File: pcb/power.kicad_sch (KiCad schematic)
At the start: 60 parts, among them J7 1S LiPo, Q1 Q_Dual_NMOS_S1G1S2G2D2D2D1D1, Q2 Q_Dual_NMOS_S1G1S2G2D2D2D1D1, Q3 Q_Dual_NMOS_S1G1S2G2D2D2D1D1, U13 BQ25798, U14 TPS63060, U15 TPS61089

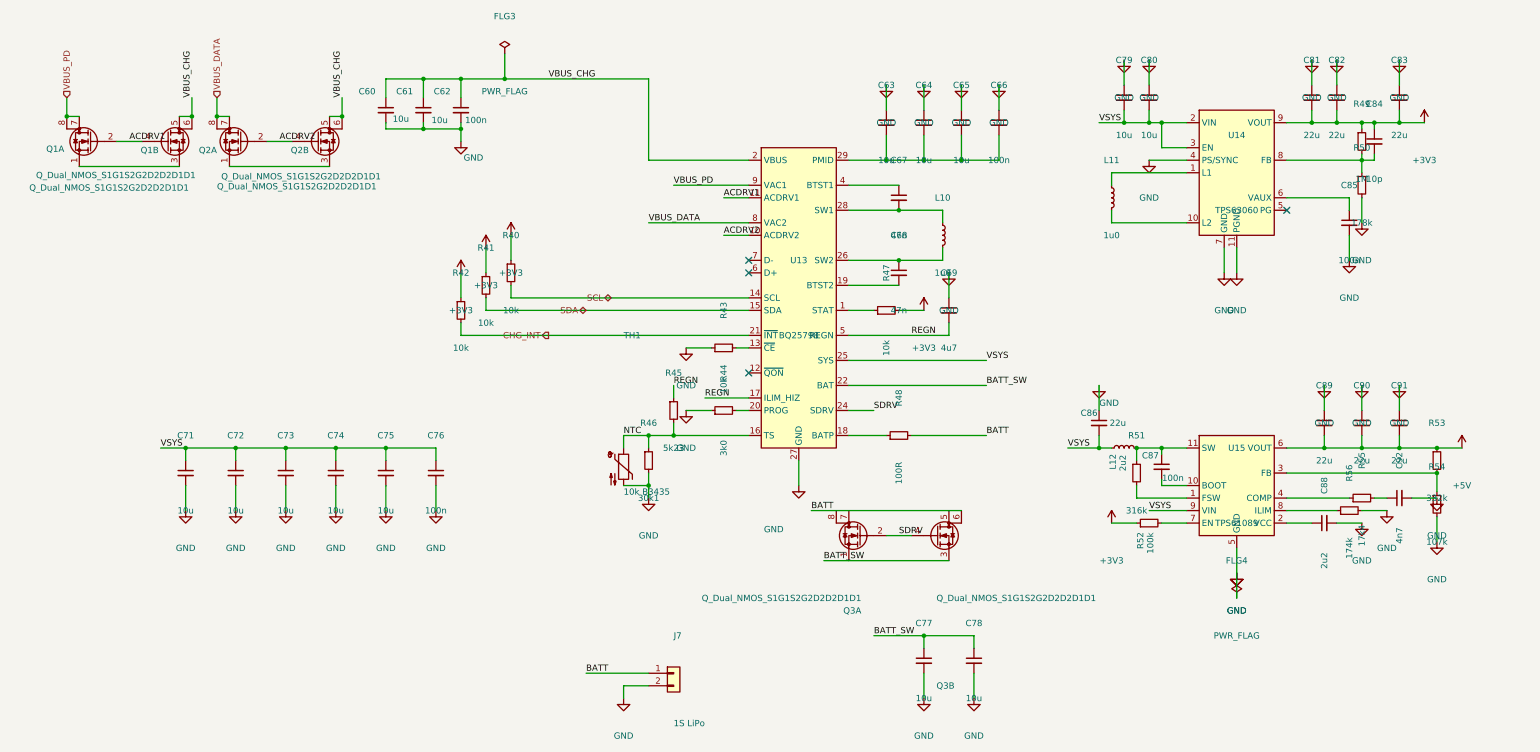
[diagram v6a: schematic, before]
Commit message: calculate the capacitor banks, and give every one of them a package
The question a value and a rating leave open is how much capacitance is actually there once the
voltage is across it, and the answer differs by package for the same value and rating. So the
requirement is derived bank by bank rather than taken from the vendors' part counts.

The charger's input is the binding case. Holding its input ripple to 100 mV with 5.4 A through the
inductor needs 8.6uF in circuit out of the 20uF fitted, so 43% has to survive 9V. The 5V rail needs
36% of what it carries and the system rail 27%. That last one is worth stating properly: ripple
alone would want only 2.5uF there, so the bank exists to answer load steps, and the realistic fast
step is the radio transmitting and the processor waking rather than the ports, which cannot step
quickly because the boost soft-starts over 4ms. At half an amp over five microseconds that is 25uF
against about 70uF effective.

43% is comfortable in 1206 and marginal in 0603 for a 10uF part at 9V, so the five capacitors on
the 9V nodes take 1206 and everything at 4.5V or under takes 0805. Decoupling goes to 0402, where
being near the pin matters more than the package, and the frequency- and loop-setting parts to
0603, where there is nothing to derate.

The answer to the open item is that the counts do not change: every bank is adequate as drawn
provided each part keeps roughly half of itself, which is what the package choice delivers. What is
left is a purchasing check rather than a design one.

Two asymmetries recorded. The 3.3V converter's vendor states that its recommended values anticipate
tolerance and bias derating and quotes 20% and 50%, so its table is nominal with the margin already
in it; the charger's and the boost's say nothing, so there the derating is ours to carry. And the
processor specifies an effective tolerance rather than a nominal one -- its core regulator's output
capacitor must be 4.7uF +/-20% in circuit.

The checker's 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
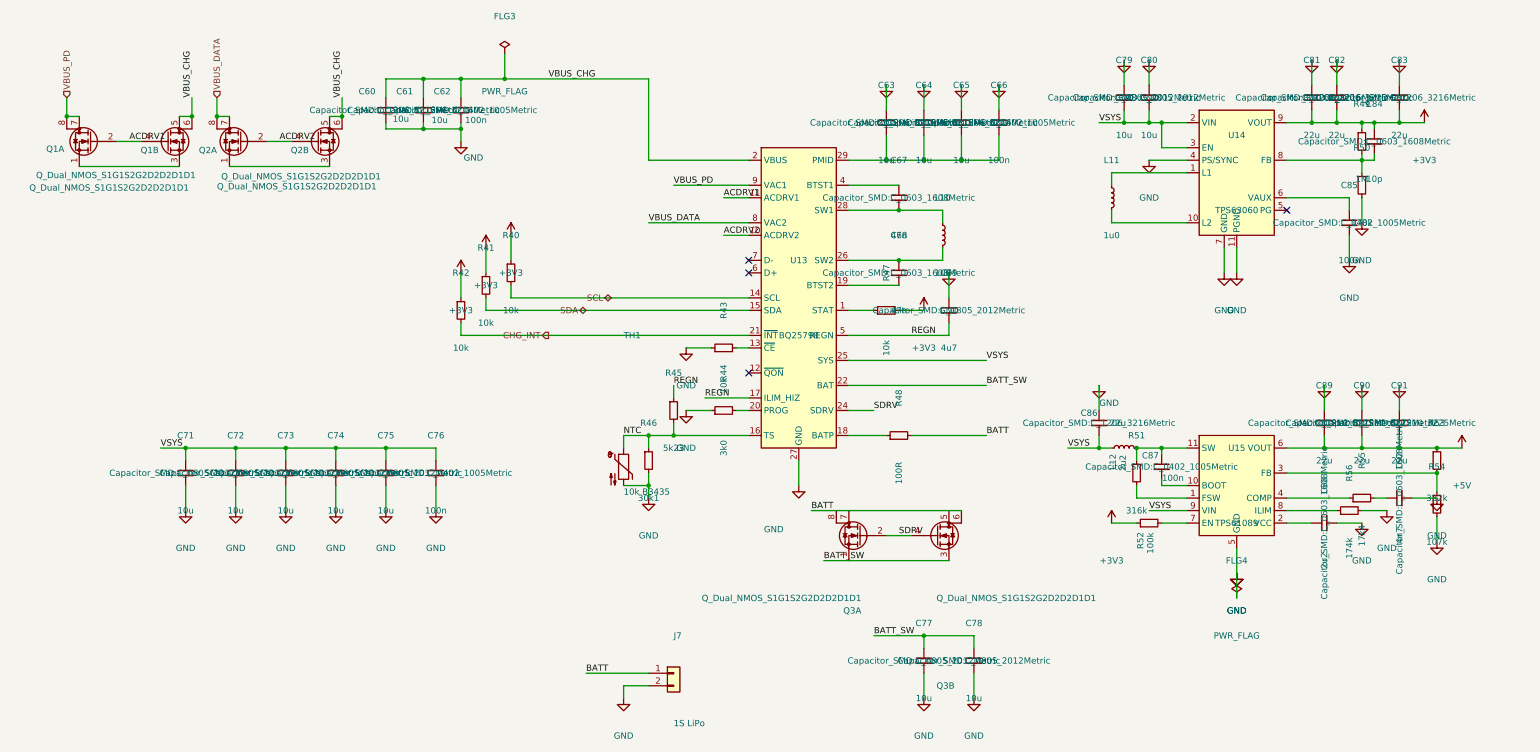
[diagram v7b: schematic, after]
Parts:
- C60, C61, C63, C64, C65, C81, C82, C83, C86: footprint (none) -> Capacitor_SMD:C_1206_3216Metric
- C62, C66, C76, C85, C87: footprint (none) -> Capacitor_SMD:C_0402_1005Metric
- C67, C68, C84, C88, C92: footprint (none) -> Capacitor_SMD:C_0603_1608Metric
- C69, C71, C72, C73, C74, C75, C77, C78, C79, C80: footprint (none) -> Capacitor_SMD:C_0805_2012Metric
- C89, C90, C91: footprint (none) -> Capacitor_SMD:C_1210_3225Metric
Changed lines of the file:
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@@
 			)
 		)
-		(property "Footprint" ""
+		(property "Footprint" "Capacitor_SMD:C_0805_2012Metric"
 			(at 248.92 86.36 0)
 			(show_name no)
@@
 			)
 		)
-		(property "Footprint" ""
+		(property "Footprint" "Capacitor_SMD:C_1206_3216Metric"
 			(at 287.02 86.36 0)
 			(show_name no)
@@
 			)
 		)
-		(property "Footprint" ""
+		(property "Footprint" "Capacitor_SMD:C_0402_1005Metric"
 			(at 289.56 111.76 0)
 			(show_name no)
@@
 			)
 		)
-		(property "Footprint" ""
+		(property "Footprint" "Capacitor_SMD:C_0603_1608Metric"
 			(at 284.48 172.72 0)
 			(show_name no)
@@
 			)
 		)
-		(property "Footprint" ""
+		(property "Footprint" "Capacitor_SMD:C_1206_3216Metric"
 			(at 238.76 152.4 0)
 			(show_name no)
@@
 			)
 		)
-		(property "Footprint" ""
+		(property "Footprint" "Capacitor_SMD:C_1210_3225Metric"
 			(at 284.48 152.4 0)
 			(show_name no)
@@
 			)
 		)
-		(property "Footprint" ""
+		(property "Footprint" "Capacitor_SMD:C_0805_2012Metric"
 			(at 203.2 200.66 0)
 			(show_name no)
@@
 			)
 		)
-		(property "Footprint" ""
+		(property "Footprint" "Capacitor_SMD:C_0603_1608Metric"
 			(at 294.64 95.25 0)
 			(show_name no)
@@
 			)
 		)
-		(property "Footprint" ""
+		(property "Footprint" "Capacitor_SMD:C_0805_2012Metric"
 			(at 83.82 162.56 0)
 			(show_name no)
@@
 			)
 		)
-		(property "Footprint" ""
+		(property "Footprint" "Capacitor_SMD:C_0402_1005Metric"
 			(at 104.14 162.56 0)
 			(show_name no)
@@
 			)
 		)
-		(property "Footprint" ""
+		(property "Footprint" "Capacitor_SMD:C_1210_3225Metric"
 			(at 299.72 152.4 0)
 			(show_name no)
@@
 			)
 		)
-		(property "Footprint" ""
+		(property "Footprint" "Capacitor_SMD:C_0805_2012Metric"
 			(at 73.66 162.56 0)
 			(show_name no)
@@
 			)
 		)
-		(property "Footprint" ""
+		(property "Footprint" "Capacitor_SMD:C_0402_1005Metric"
 			(at 251.46 161.29 0)
 			(show_name no)
@@
 			)
 		)
-		(property "Footprint" ""
+		(property "Footprint" "Capacitor_SMD:C_1206_3216Metric"
 			(at 195.58 91.44 0)
 			(show_name no)
@@
 			)
 		)
-		(property "Footprint" ""
+		(property "Footprint" "Capacitor_SMD:C_0805_2012Metric"
 			(at 243.84 86.36 0)
 			(show_name no)
@@
 			)
 		)
-		(property "Footprint" ""
+		(property "Footprint" "Capacitor_SMD:C_1210_3225Metric"
 			(at 292.1 152.4 0)
 			(show_name no)
@@
 			)
 		)
-		(property "Footprint" ""
+		(property "Footprint" "Capacitor_SMD:C_0402_1005Metric"
 			(at 218.44 91.44 0)
 			(show_name no)
@@
 			)
 		)
-		(property "Footprint" ""
+		(property "Footprint" "Capacitor_SMD:C_1206_3216Metric"
 			(at 93.98 88.9 0)
 			(show_name no)
@@
 			)
 		)
-		(property "Footprint" ""
+		(property "Footprint" "Capacitor_SMD:C_0805_2012Metric"
 			(at 93.98 162.56 0)
 			(show_name no)
@@
 			)
 		)
-		(property "Footprint" ""
+		(property "Footprint" "Capacitor_SMD:C_1206_3216Metric"
 			(at 203.2 91.44 0)
 			(show_name no)
@@
 			)
 		)
-		(property "Footprint" ""
+		(property "Footprint" "Capacitor_SMD:C_0402_1005Metric"
 			(at 109.22 88.9 0)
 			(show_name no)
@@
 			)
 		)
-		(property "Footprint" ""
+		(property "Footprint" "Capacitor_SMD:C_0805_2012Metric"
 			(at 53.34 162.56 0)
 			(show_name no)
@@
 			)
 		)
-		(property "Footprint" ""
+		(property "Footprint" "Capacitor_SMD:C_0805_2012Metric"
 			(at 213.36 200.66 0)
 			(show_name no)
@@
 			)
 		)
-		(property "Footprint" ""
+		(property "Footprint" "Capacitor_SMD:C_1206_3216Metric"
 			(at 299.72 86.36 0)
 			(show_name no)
@@
 			)
 		)
-		(property "Footprint" ""
+		(property "Footprint" "Capacitor_SMD:C_0603_1608Metric"
 			(at 299.72 167.64 0)
 			(show_name no)
@@
 			)
 		)
-		(property "Footprint" ""
+		(property "Footprint" "Capacitor_SMD:C_0805_2012Metric"
 			(at 208.28 129.54 0)
 			(show_name no)
@@
 			)
 		)
-		(property "Footprint" ""
+		(property "Footprint" "Capacitor_SMD:C_1206_3216Metric"
 			(at 281.94 86.36 0)
 			(show_name no)
@@
 			)
 		)
-		(property "Footprint" ""
+		(property "Footprint" "Capacitor_SMD:C_0805_2012Metric"
 			(at 63.5 162.56 0)
 			(show_name no)
@@
 			)
 		)
-		(property "Footprint" ""
+		(property "Footprint" "Capacitor_SMD:C_1206_3216Metric"
 			(at 101.6 88.9 0)
 			(show_name no)
@@
 			)
 		)
-		(property "Footprint" ""
+		(property "Footprint" "Capacitor_SMD:C_1206_3216Metric"
 			(at 210.82 91.44 0)
 			(show_name no)
@@
 			)
 		)
-		(property "Footprint" ""
+		(property "Footprint" "Capacitor_SMD:C_0603_1608Metric"
 			(at 198.12 106.68 0)
 			(show_name no)
@@
 			)
 		)
-		(property "Footprint" ""
+		(property "Footprint" "Capacitor_SMD:C_0603_1608Metric"
 			(at 198.12 121.92 0)
 			(show_name no)

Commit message: assign the footprints, and take the radio module's from its vendor
132 of the 135 parts now carry a footprint. Most follow from the package, the capacitors' follow
from the bias calculation, and the resistors are 0603 rather than 0402 because the board has room,
the first one runs bare on a bench, and a part you can get a probe or an iron onto is worth more
there than the millimetre it saves.

The radio module nearly went in hand-drawn. It has no footprint in any stock library, so the
obvious move was to draw one from the dimension drawing in its datasheet; the pitch, pad size and
pad length read off cleanly, but where each pad sits along its edge did not, and what I had was
inference from where things appeared in a rendered figure rather than a stated number. Raspberry Pi
publish a KiCad symbol and footprint, so that is what is fitted, in a project footprint library
beside the project symbol library. The figure agreed on everything it stated plainly, which says
nothing about the parts it did not.

Taking the official symbol also checked this project's hand-drawn one against theirs. All 21 pins
agree. Four carry different names -- their DI and DO, their nIRQ and WL_ON -- and nothing else
differs, so the pin numbering derived from the module's table is confirmed against its author
rather than merely self-consistent.

Four packages are fitted provisionally and are recorded as such, because what is unsettled about
them is invisible: the processor, the hub, the 3.3V converter and the power sink are in packages
whose library entries differ only in the size of the pad under the part. Body, pitch and pin count
are right; the pad is the nearest variant and wants checking against each vendor's land pattern,
since too small costs thermal performance and too large can wick the part off its pins.

Three parts are deliberately left without one. For the remaining inductors the footprint is the
part -- pad geometry differs between vendors at the same nominal size -- so choosing an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
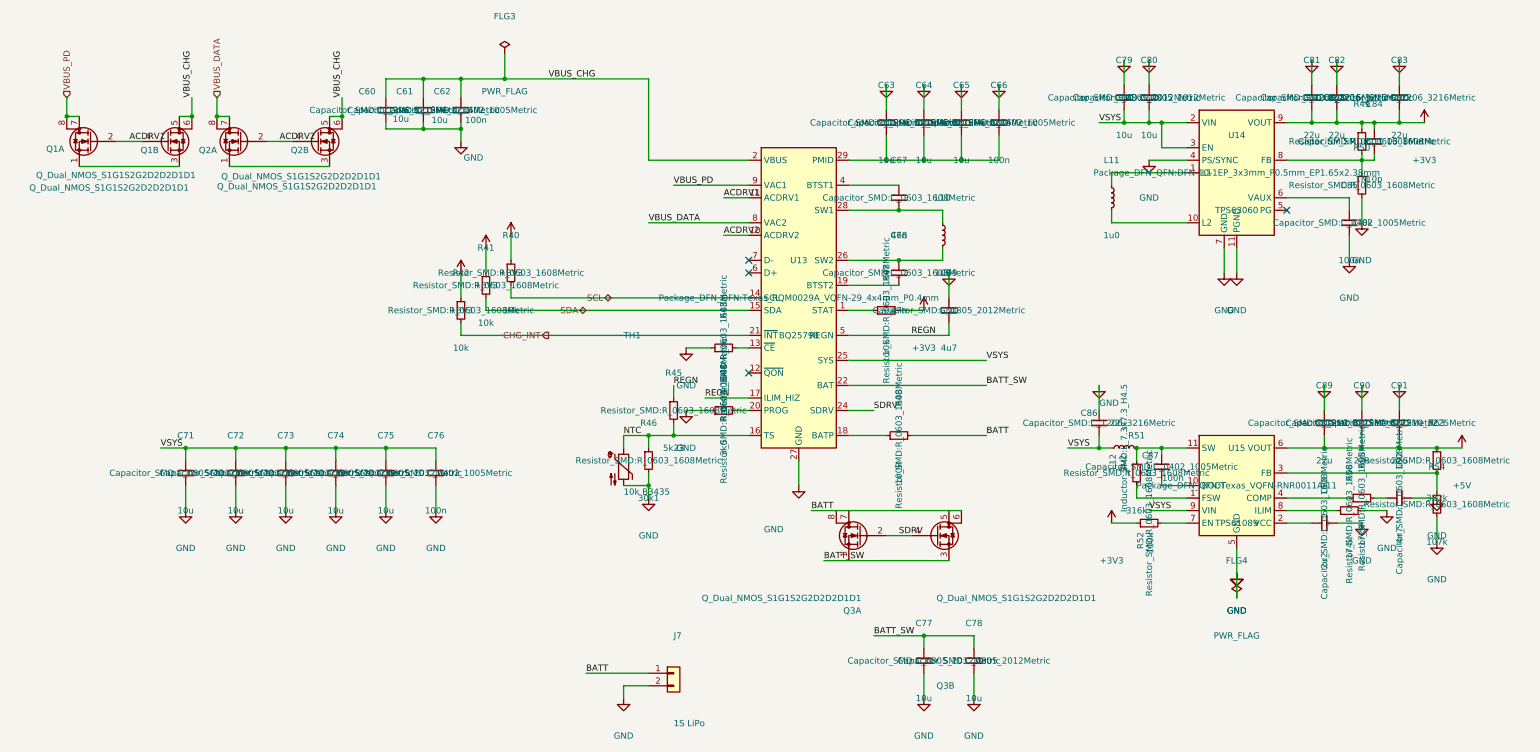
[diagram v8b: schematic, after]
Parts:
- J7: footprint (none) -> Connector_JST:JST_PH_B2B-PH-K_1x02_P2.00mm_Vertical
- L12: footprint (none) -> Inductor_SMD:L_7.3x7.3_H4.5
- Q1, Q2, Q3: footprint (none) -> Package_SO:SOIC-8_3.9x4.9mm_P1.27mm
- R40, R41, R42, R43, R44, R45, R46, R47, R48, R49, R50, R51, R52, R53, R54, R55, R56, TH1: footprint (none) -> Resistor_SMD:R_0603_1608Metric
- U13: footprint (none) -> Package_DFN_QFN:Texas_RQM0029A_VQFN-29_4x4mm_P0.4mm
- U14: footprint (none) -> Package_DFN_QFN:DFN-10-1EP_3x3mm_P0.5mm_EP1.65x2.38mm
- U15: footprint (none) -> Package_DFN_QFN:Texas_VQFN-RNR0011A-11
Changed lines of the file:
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@@
 			)
 		)
-		(property "Footprint" ""
+		(property "Footprint" "Resistor_SMD:R_0603_1608Metric"
 			(at 307.34 160.02 0)
 			(show_name no)
@@
 			)
 		)
-		(property "Footprint" ""
+		(property "Footprint" "Resistor_SMD:R_0603_1608Metric"
 			(at 248.92 172.72 0)
 			(show_name no)
@@
 			)
 		)
-		(property "Footprint" ""
+		(property "Footprint" "Resistor_SMD:R_0603_1608Metric"
 			(at 119.38 121.92 0)
 			(show_name no)
@@
 			)
 		)
-		(property "Footprint" ""
+		(property "Footprint" "Package_SO:SOIC-8_3.9x4.9mm_P1.27mm"
 			(at 34.29 95.25 0)
 			(hide yes)
@@
 			)
 		)
-		(property "Footprint" ""
+		(property "Footprint" "Resistor_SMD:R_0603_1608Metric"
 			(at 152.4 149.86 0)
 			(show_name no)
@@
 			)
 		)
-		(property "Footprint" ""
+		(property "Footprint" "Resistor_SMD:R_0603_1608Metric"
 			(at 292.1 95.25 0)
 			(show_name no)
@@
 			)
 		)
-		(property "Footprint" ""
+		(property "Footprint" "Resistor_SMD:R_0603_1608Metric"
 			(at 292.1 167.64 0)
 			(show_name no)
@@
 			)
 		)
-		(property "Footprint" ""
+		(property "Footprint" "Package_SO:SOIC-8_3.9x4.9mm_P1.27mm"
 			(at 64.77 95.25 0)
 			(hide yes)
@@
 			)
 		)
-		(property "Footprint" ""
+		(property "Footprint" "Resistor_SMD:R_0603_1608Metric"
 			(at 162.56 137.16 0)
 			(show_name no)
@@
 			)
 		)
-		(property "Footprint" ""
+		(property "Footprint" "Inductor_SMD:L_7.3x7.3_H4.5"
 			(at 243.84 157.48 0)
 			(show_name no)
@@
 			)
 		)
-		(property "Footprint" ""
+		(property "Footprint" "Resistor_SMD:R_0603_1608Metric"
 			(at 147.32 160.02 0)
 			(show_name no)
@@
 			)
 		)
-		(property "Footprint" ""
+		(property "Footprint" "Resistor_SMD:R_0603_1608Metric"
 			(at 195.58 129.54 0)
 			(show_name no)
@@
 			)
 		)
-		(property "Footprint" ""
+		(property "Footprint" "Resistor_SMD:R_0603_1608Metric"
 			(at 198.12 154.94 0)
 			(show_name no)
@@
 			)
 		)
-		(property "Footprint" ""
+		(property "Footprint" "Resistor_SMD:R_0603_1608Metric"
 			(at 114.3 124.46 0)
 			(show_name no)
@@
 			)
 		)
-		(property "Footprint" ""
+		(property "Footprint" "Resistor_SMD:R_0603_1608Metric"
 			(at 109.22 129.54 0)
 			(show_name no)
@@
 			)
 		)
-		(property "Footprint" ""
+		(property "Footprint" "Package_SO:SOIC-8_3.9x4.9mm_P1.27mm"
 			(at 49.53 95.25 0)
 			(hide yes)
@@
 			)
 		)
-		(property "Footprint" ""
+		(property "Footprint" "Resistor_SMD:R_0603_1608Metric"
 			(at 246.38 162.56 0)
 			(show_name no)
@@
 			)
 		)
-		(property "Footprint" ""
+		(property "Footprint" "Package_DFN_QFN:Texas_VQFN-RNR0011A-11"
 			(at 266.7 165.1 0)
 			(show_name no)
@@
 			)
 		)
-		(property "Footprint" ""
+		(property "Footprint" "Resistor_SMD:R_0603_1608Metric"
 			(at 289.56 170.18 0)
 			(show_name no)
@@
 			)
 		)
-		(property "Footprint" ""
+		(property "Footprint" "Package_SO:SOIC-8_3.9x4.9mm_P1.27mm"
 			(at 80.01 95.25 0)
 			(hide yes)
@@
 			)
 		)
-		(property "Footprint" ""
+		(property "Footprint" "Resistor_SMD:R_0603_1608Metric"
 			(at 307.34 168.91 0)
 			(show_name no)
@@
 			)
 		)
-		(property "Footprint" ""
+		(property "Footprint" "Resistor_SMD:R_0603_1608Metric"
 			(at 162.56 149.86 0)
 			(show_name no)
@@
 			)
 		)
-		(property "Footprint" ""
+		(property "Footprint" "Package_DFN_QFN:DFN-10-1EP_3x3mm_P0.5mm_EP1.65x2.38mm"
 			(at 266.7 101.6 0)
 			(show_name no)
@@
 			)
 		)
-		(property "Footprint" ""
+		(property "Footprint" "Package_DFN_QFN:Texas_RQM0029A_VQFN-29_4x4mm_P0.4mm"
 			(at 177.8 127 0)
 			(show_name no)
@@
 			)
 		)
-		(property "Footprint" ""
+		(property "Footprint" "Resistor_SMD:R_0603_1608Metric"
 			(at 292.1 104.14 0)
 			(show_name no)
@@
 			)
 		)
-		(property "Footprint" ""
+		(property "Footprint" "Package_SO:SOIC-8_3.9x4.9mm_P1.27mm"
 			(at 190.50 175.26 0)
 			(show_name no)
@@
 			)
 		)
-		(property "Footprint" ""
+		(property "Footprint" "Package_SO:SOIC-8_3.9x4.9mm_P1.27mm"
 			(at 205.74 175.26 0)
 			(show_name no)
@@
 			)
 		)
-		(property "Footprint" ""
+		(property "Footprint" "Connector_JST:JST_PH_B2B-PH-K_1x02_P2.00mm_Vertical"
 			(at 152.40 203.20 0)
 			(show_name no)
@@
 			)
 		)
-		(property "Footprint" ""
+		(property "Footprint" "Resistor_SMD:R_0603_1608Metric"
 			(at 142.24 161.29 0)
 			(show_name no)
